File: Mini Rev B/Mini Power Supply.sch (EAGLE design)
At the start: 29 parts

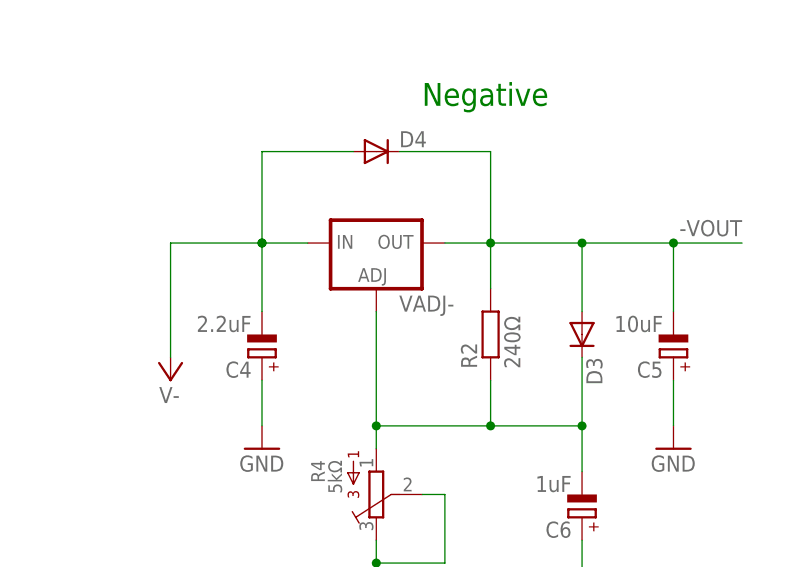
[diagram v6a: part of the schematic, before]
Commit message: Fixed the negative voltage regulator
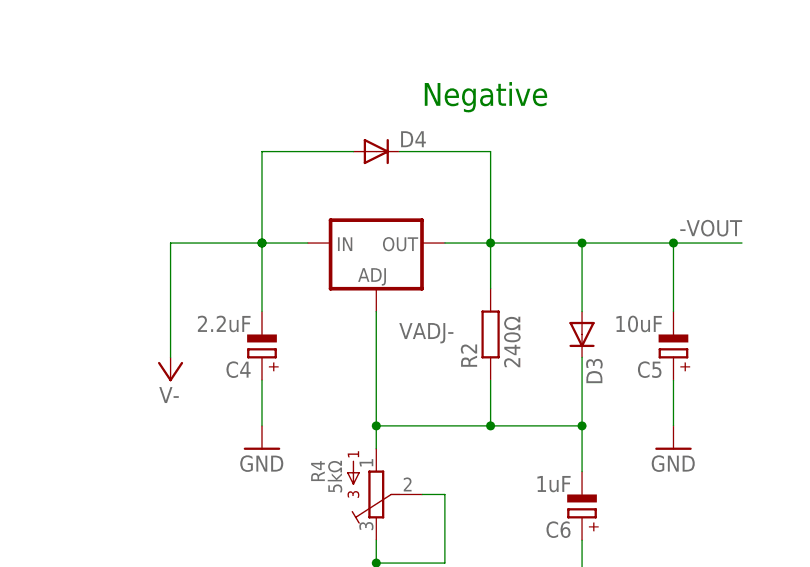
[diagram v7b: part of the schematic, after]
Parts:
- VADJ-: device v-reg:LM317L -> v-reg:LM337L
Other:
- moved on the sheet: VADJ-
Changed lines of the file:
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@@
 <part name="R4" library="bourns" deviceset="3386-" device="U" value="5kΩ"/>
 <part name="VADJ+" library="v-reg" deviceset="LM317L" device=""/>
-<part name="VADJ-" library="v-reg" deviceset="LM317L" device=""/>
+<part name="VADJ-" library="v-reg" deviceset="LM337L" device=""/>
 </parts>
 <sheets>
@@
 <instance part="R4" gate="G$1" x="124.46" y="0" rot="MR180"/>
 <instance part="VADJ+" gate="A" x="124.46" y="114.3"/>
-<instance part="VADJ-" gate="A" x="124.46" y="27.94"/>
+<instance part="VADJ-" gate="A" x="124.46" y="27.94" rot="MR180"/>
 </instances>
 <busses>
